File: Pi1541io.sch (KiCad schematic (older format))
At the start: 41 parts, among them J1 IEC1, J2 IEC2, J3 IEC3, J4 ExtSpkr, J5 GS3, J6 GS3, J7 GS3, J8 GS3, P1 Conn_02x20_Odd_Even, Q1 BSS138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

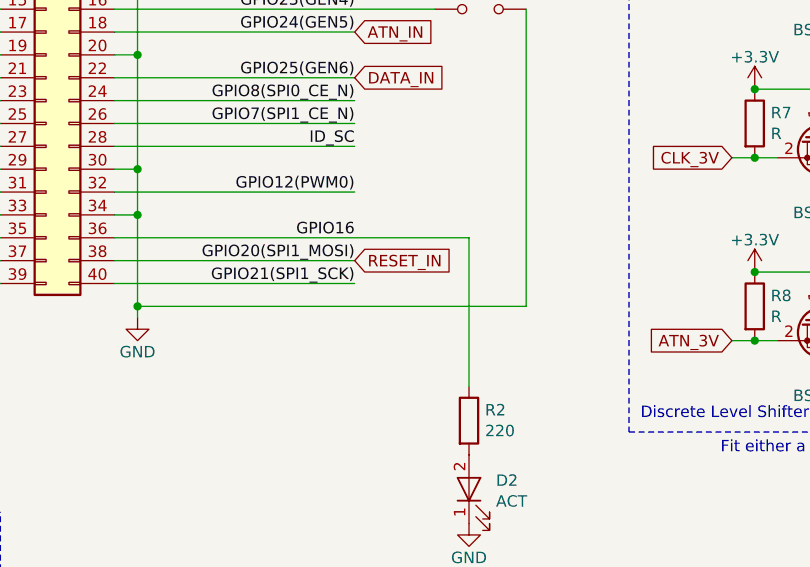
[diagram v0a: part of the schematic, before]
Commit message: Added SRQ label.
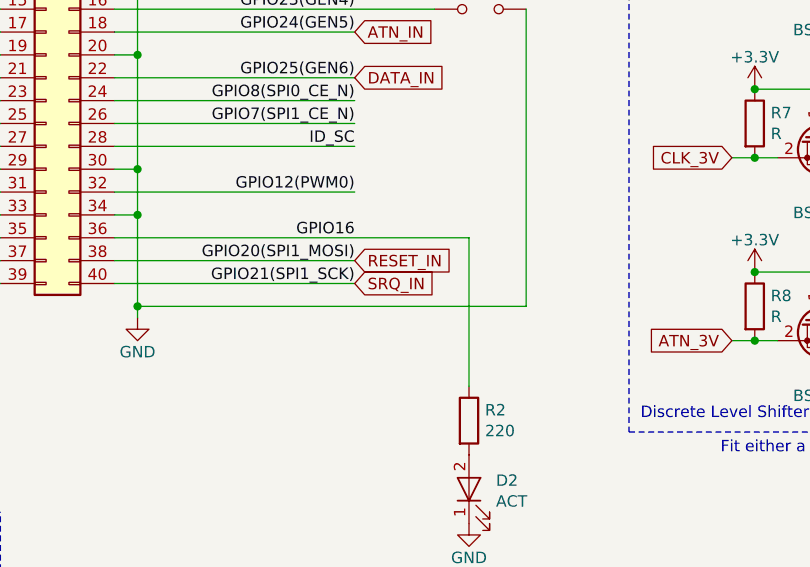
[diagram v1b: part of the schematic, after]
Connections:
- net GPIO21(SPI1_SCK) renamed SRQ_IN
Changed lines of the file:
@@
 Text Notes 6650 4050 0    50   ~ 0
 Fit either a compatible level shifter module OR the discrete components!
+Text GLabel 5050 3300 2    50   Input ~ 0
+SRQ_IN
 $EndSCHEMATC

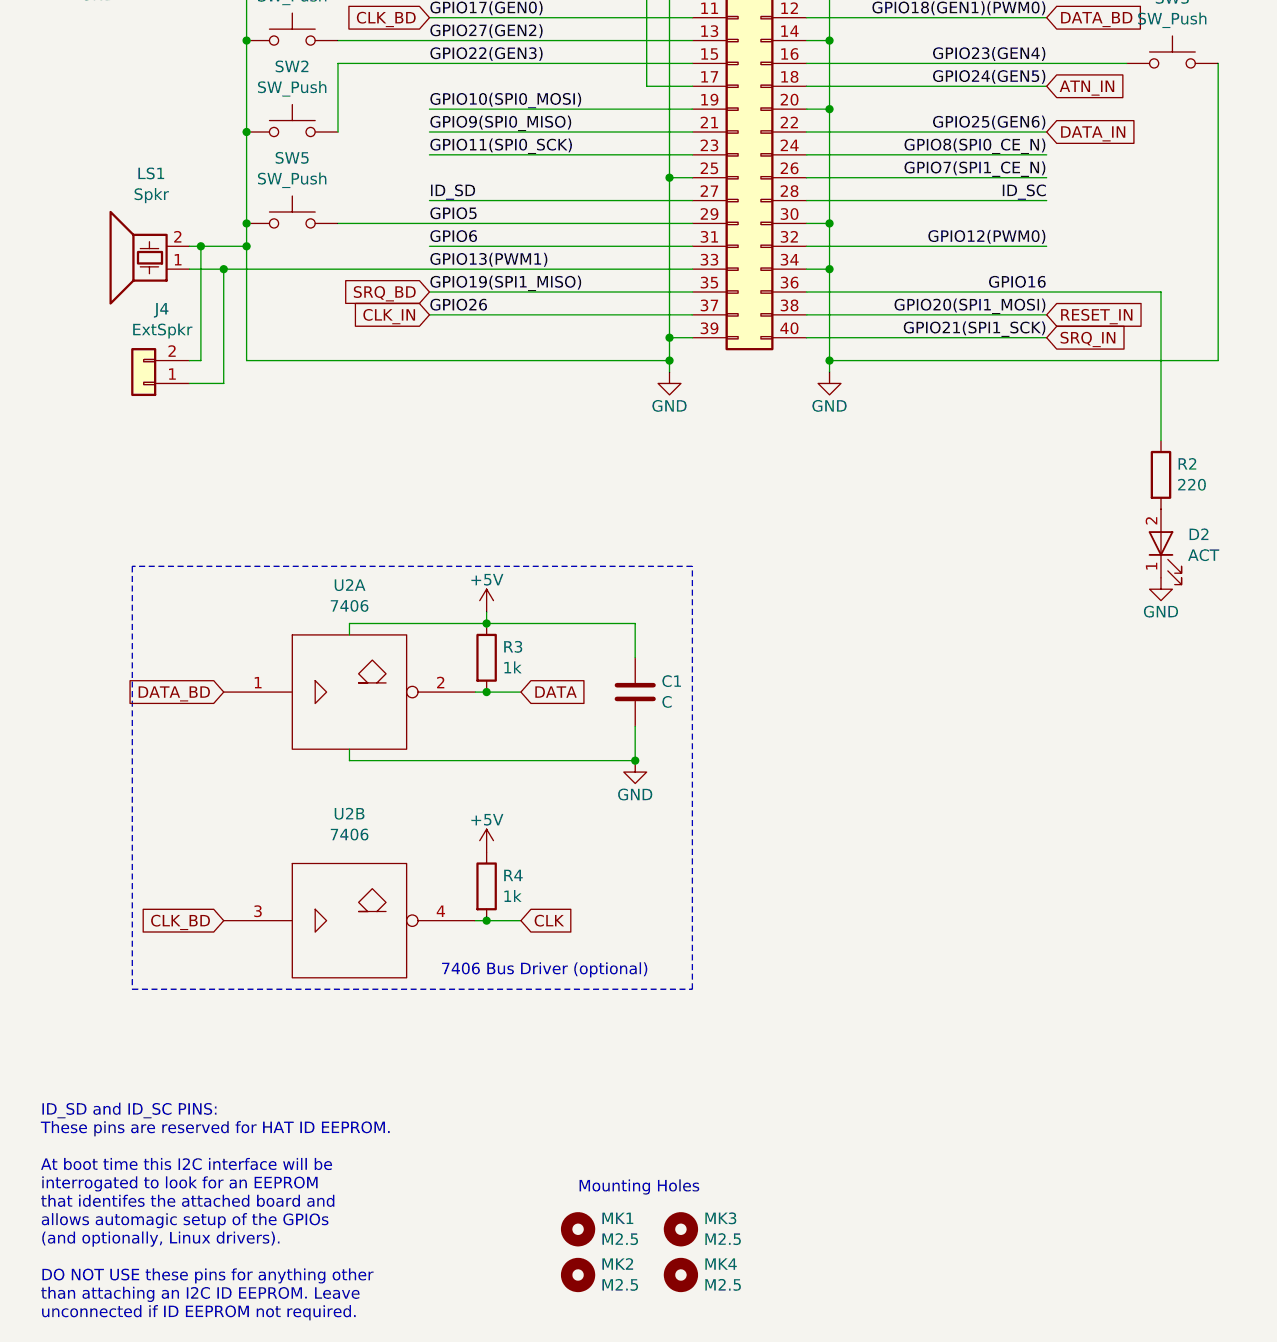
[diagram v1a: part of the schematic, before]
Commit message: Added optional components for reserved SRQ pins.
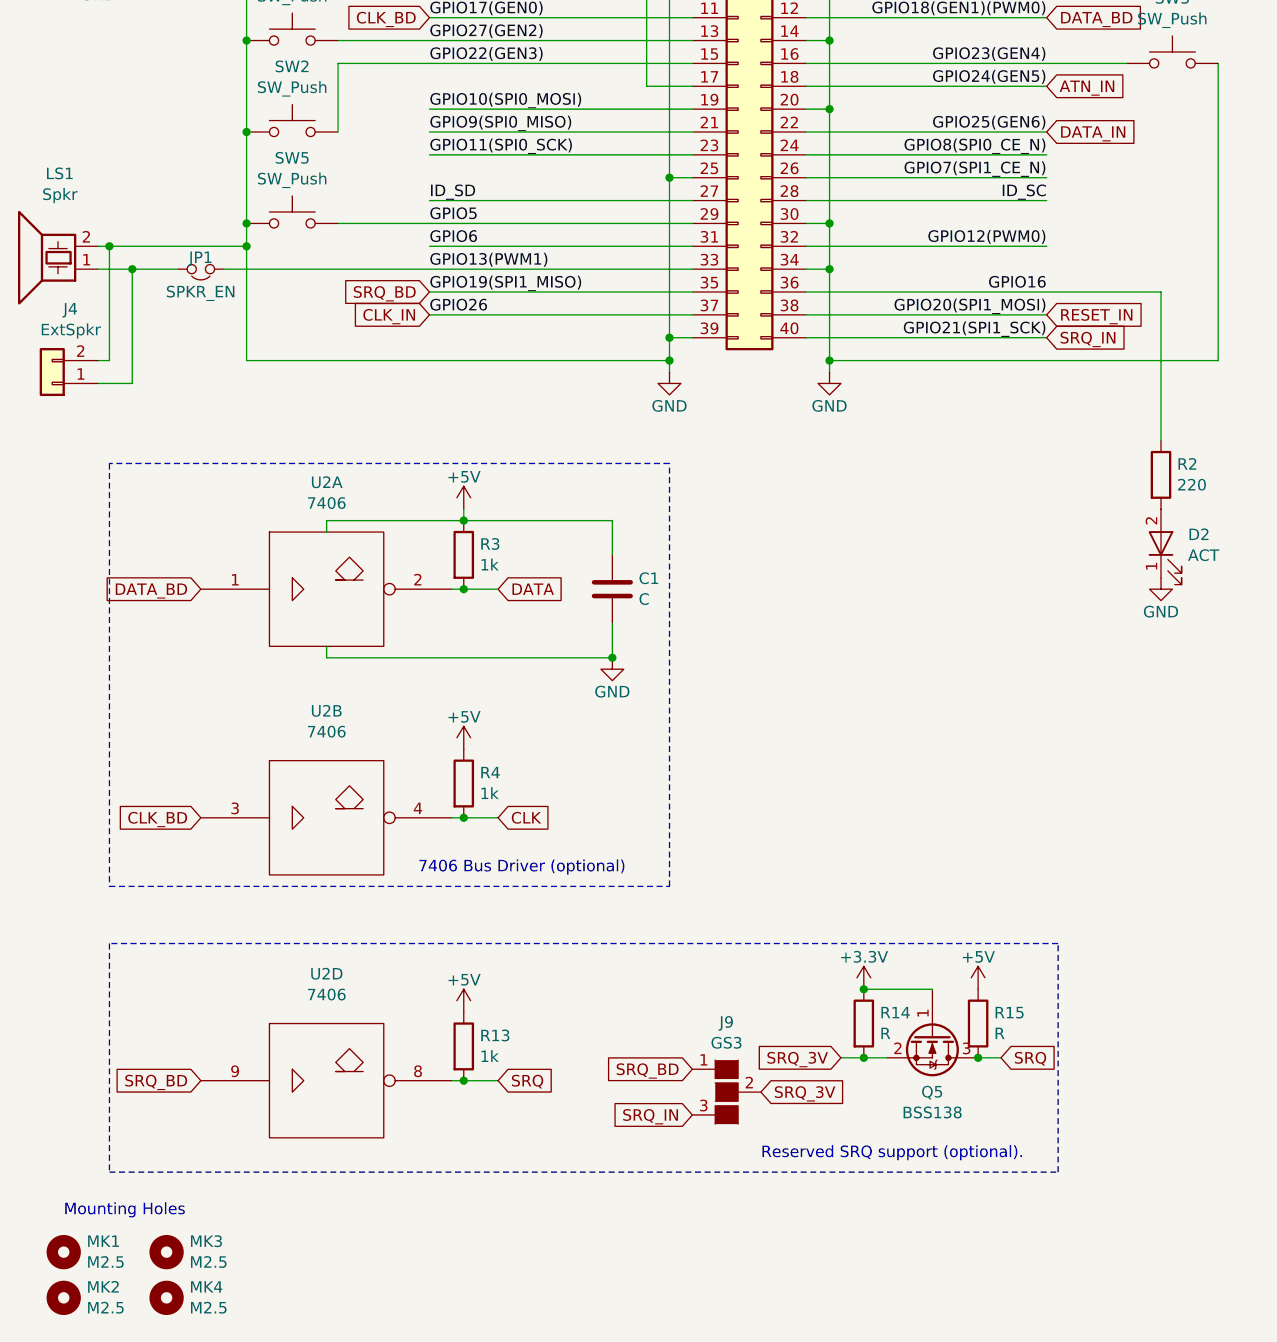
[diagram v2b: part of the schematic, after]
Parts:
- added J9: GS3, Connectors:GS3, symbol conn:GS3
- added JP1: SPKR_EN, Pin_Headers:Pin_Header_Straight_1x02_Pitch2.54mm, symbol device:Jumper_NC_Small
- added Q5: BSS138, TO_SOT_Packages_SMD:SOT-23, symbol Transistor:BSS138
- added R13: 1k, Resistors_SMD:R_0805_HandSoldering, symbol device:R
- added R14, R15: R, Resistors_SMD:R_0805, symbol device:R
- added unit 4 of U2
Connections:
- net +3V3: now also Q5.1 (G), R14.1
- net +5V: now also R13.1, R15.1, U2.14 (Vcc)
- net GND: now also U2.7 (Gnd)
- net GPIO13(PWM1): now also JP1.1; no longer J4.1 (Pin_1), LS1.1
- net SRQ: now also Q5.3 (D), R13.2, R15.2, U2.8
- net SRQ_BD: now also J9.1 (G1), U2.9
- net SRQ_IN: now also J9.3 (G3)
- new net: J4.1 (Pin_1), JP1.2, LS1.1
- new net SRQ_3V: J9.2 (G2), Q5.2 (S), R14.2
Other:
- note added: "Reserved SRQ support (optional)."
- note removed: "ID_SD and ID_SC PINS:\nThese pins are reserved for HAT ID EEPROM.\n\nAt boot time this I2C interface will be\ninterrogated to look for an EEPROM\nthat identifes the attached board and\nallows automagic setup of the GPIOs\n(and optionally, Linux drivers).\n\nDO NOT USE these pins for anything other\nthan attaching an I2C ID EEPROM. Leave\nunconnected if ID EEPROM not required."
- moved on the sheet: C1, J4, LS1, MK1, MK2, MK3, MK4, R3, R4, U2A, U2B

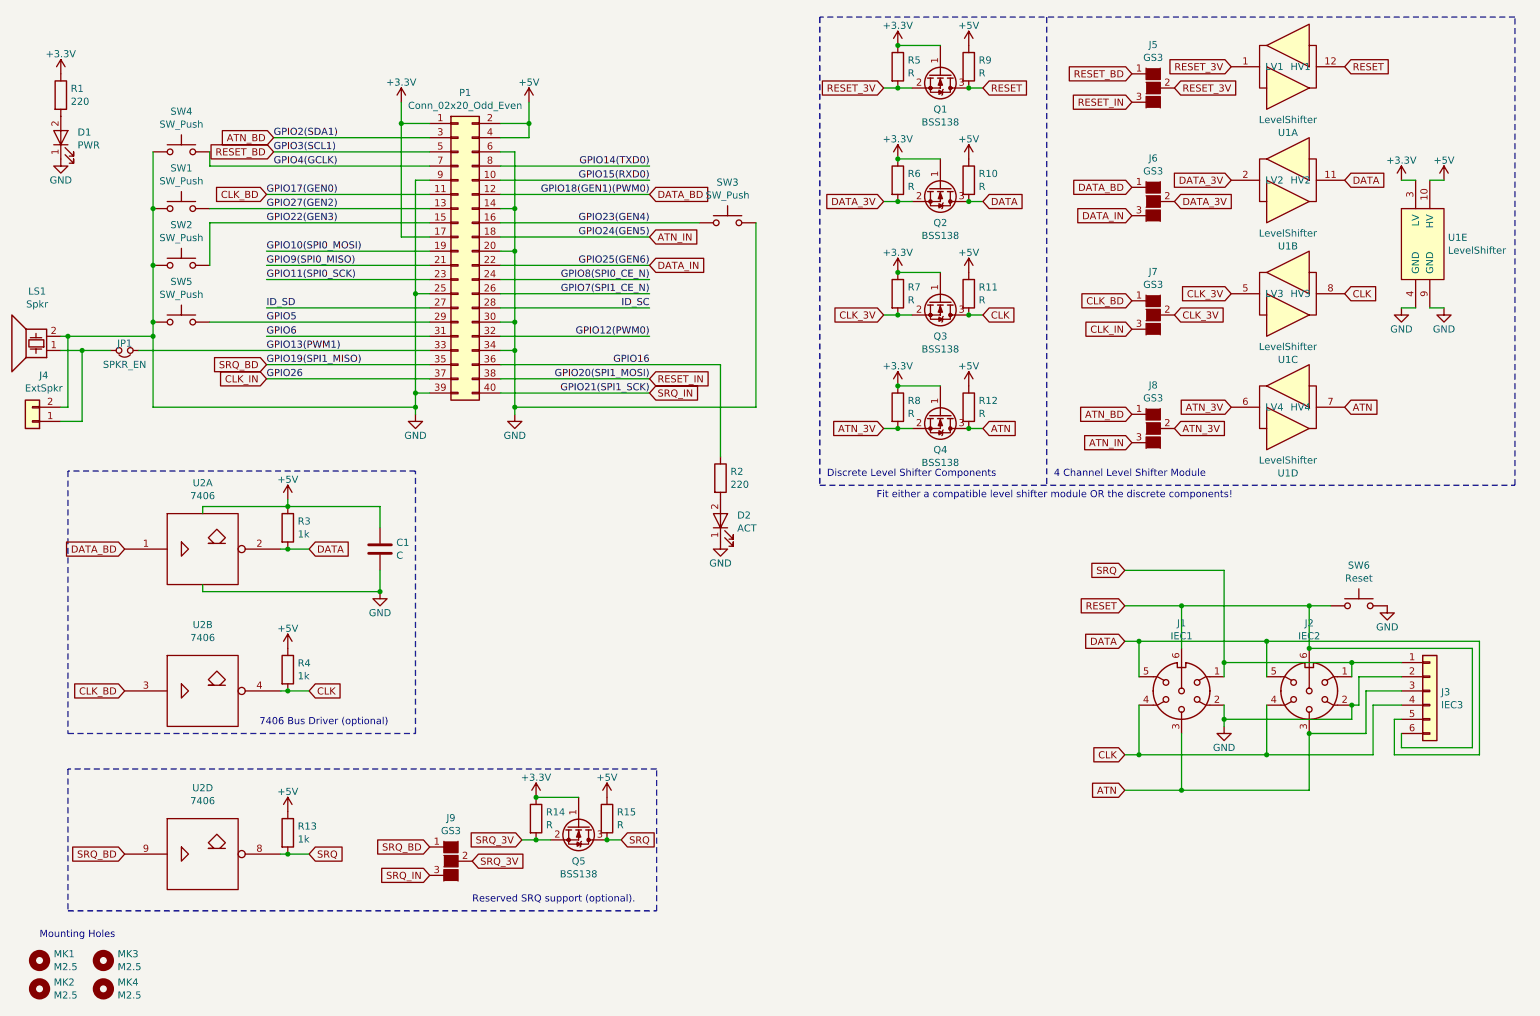
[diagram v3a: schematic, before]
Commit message: Added missing values.
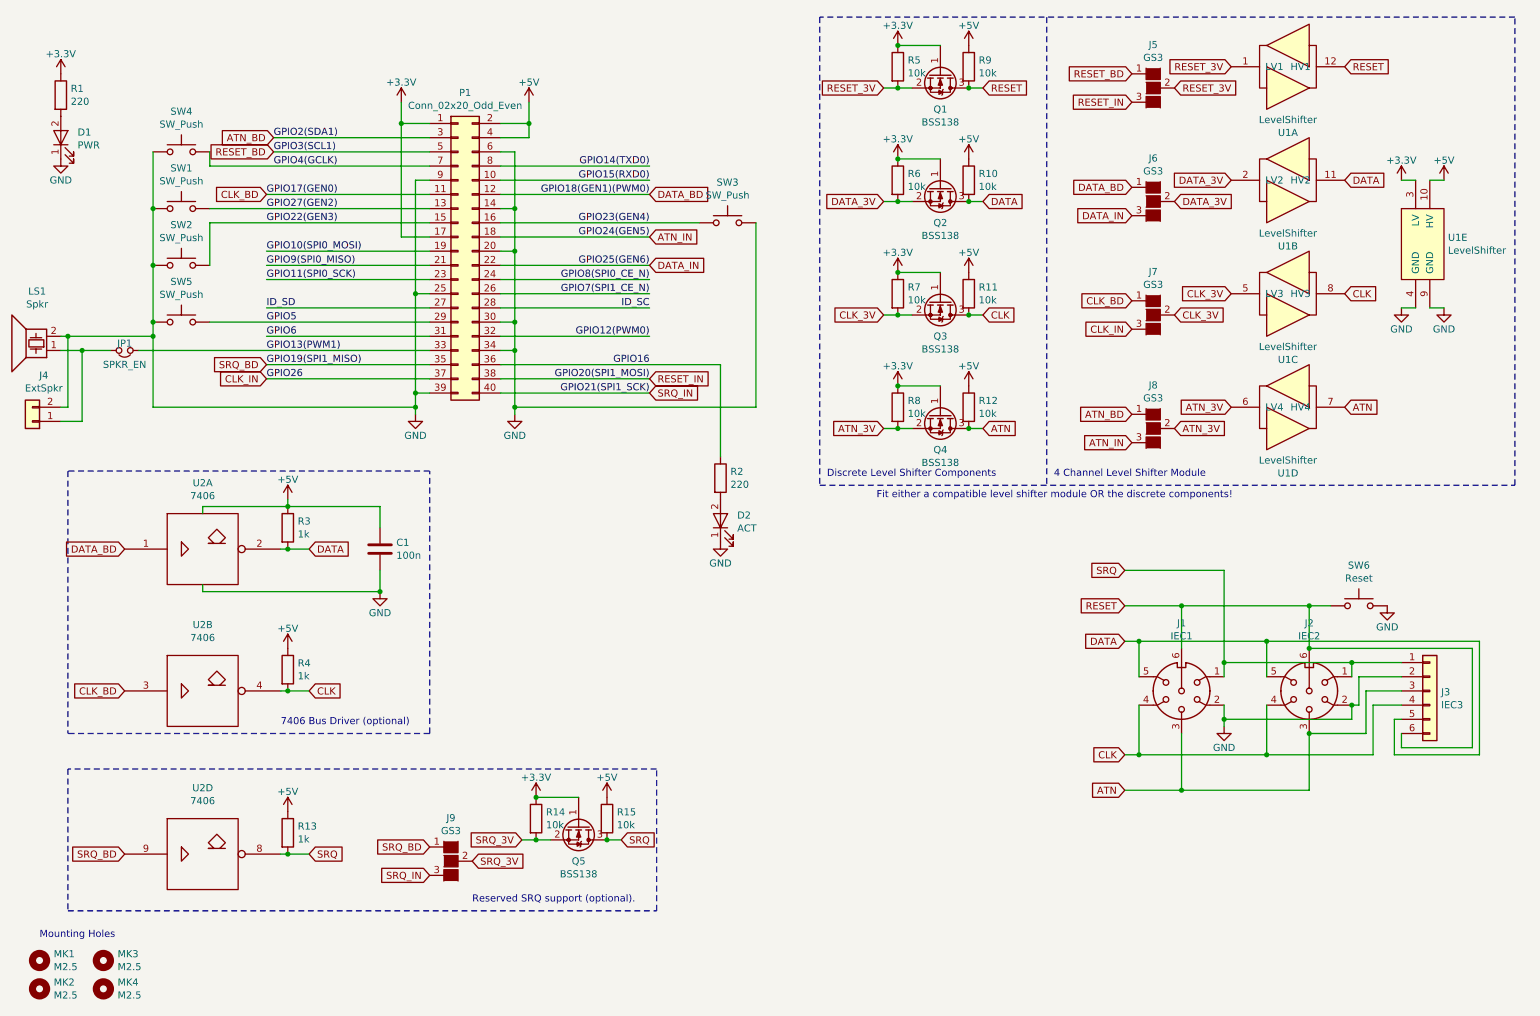
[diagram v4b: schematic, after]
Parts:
- C1: value C -> 100n
- R10, R11, R12, R14, R15, R5, R6, R7, R8, R9: value R -> 10k
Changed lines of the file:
@@
 P 3150 4400
 F 0 "C1" H 3265 4446 50  0000 L CNN
-F 1 "C" H 3265 4355 50  0000 L CNN
+F 1 "100n" H 3265 4355 50  0000 L CNN
 F 2 "Capacitors_THT:C_Disc_D3.0mm_W1.6mm_P2.50mm" H 3188 4250 50  0001 C CNN
 F 3 "" H 3150 4400 50  0001 C CNN
@@
 P 6800 1000
 F 0 "R5" H 6870 1046 50  0000 L CNN
-F 1 "R" H 6870 955 50  0000 L CNN
+F 1 "10k" H 6870 955 50  0000 L CNN
 F 2 "Resistors_SMD:R_0805" V 6730 1000 50  0001 C CNN
 F 3 "" H 6800 1000 50  0001 C CNN
@@
 P 7300 1000
 F 0 "R9" H 7370 1046 50  0000 L CNN
-F 1 "R" H 7370 955 50  0000 L CNN
+F 1 "10k" H 7370 955 50  0000 L CNN
 F 2 "Resistors_SMD:R_0805" V 7230 1000 50  0001 C CNN
 F 3 "" H 7300 1000 50  0001 C CNN
@@
 P 6800 1800
 F 0 "R6" H 6870 1846 50  0000 L CNN
-F 1 "R" H 6870 1755 50  0000 L CNN
+F 1 "10k" H 6870 1755 50  0000 L CNN
 F 2 "Resistors_SMD:R_0805" V 6730 1800 50  0001 C CNN
 F 3 "" H 6800 1800 50  0001 C CNN
@@
 P 7300 1800
 F 0 "R10" H 7370 1846 50  0000 L CNN
-F 1 "R" H 7370 1755 50  0000 L CNN
+F 1 "10k" H 7370 1755 50  0000 L CNN
 F 2 "Resistors_SMD:R_0805" V 7230 1800 50  0001 C CNN
 F 3 "" H 7300 1800 50  0001 C CNN
@@
 P 6800 2600
 F 0 "R7" H 6870 2646 50  0000 L CNN
-F 1 "R" H 6870 2555 50  0000 L CNN
+F 1 "10k" H 6870 2555 50  0000 L CNN
 F 2 "Resistors_SMD:R_0805" V 6730 2600 50  0001 C CNN
 F 3 "" H 6800 2600 50  0001 C CNN
@@
 P 7300 2600
 F 0 "R11" H 7370 2646 50  0000 L CNN
-F 1 "R" H 7370 2555 50  0000 L CNN
+F 1 "10k" H 7370 2555 50  0000 L CNN
 F 2 "Resistors_SMD:R_0805" V 7230 2600 50  0001 C CNN
 F 3 "" H 7300 2600 50  0001 C CNN
@@
 P 6800 3400
 F 0 "R8" H 6870 3446 50  0000 L CNN
-F 1 "R" H 6870 3355 50  0000 L CNN
+F 1 "10k" H 6870 3355 50  0000 L CNN
 F 2 "Resistors_SMD:R_0805" V 6730 3400 50  0001 C CNN
 F 3 "" H 6800 3400 50  0001 C CNN
@@
 P 7300 3400
 F 0 "R12" H 7370 3446 50  0000 L CNN
-F 1 "R" H 7370 3355 50  0000 L CNN
+F 1 "10k" H 7370 3355 50  0000 L CNN
 F 2 "Resistors_SMD:R_0805" V 7230 3400 50  0001 C CNN
 F 3 "" H 7300 3400 50  0001 C CNN
@@
 Discrete Level Shifter Components
 Wire Notes Line
-	3400 3850 950  3850
-Wire Notes Line
 	950  3850 950  5700
 Wire Notes Line
-	950  5700 3400 5700
-Wire Notes Line
-	3400 5700 3400 3850
-Text Notes 2300 5650 0    50   ~ 0
+	3500 5700 3500 3850
+Text Notes 2450 5650 0    50   ~ 0
 7406 Bus Driver (optional)
 Text Notes 6650 4050 0    50   ~ 0
@@
 P 4250 6300
 F 0 "R14" H 4320 6346 50  0000 L CNN
-F 1 "R" H 4320 6255 50  0000 L CNN
+F 1 "10k" H 4320 6255 50  0000 L CNN
 F 2 "Resistors_SMD:R_0805" V 4180 6300 50  0001 C CNN
 F 3 "" H 4250 6300 50  0001 C CNN
@@
 P 4750 6300
 F 0 "R15" H 4820 6346 50  0000 L CNN
-F 1 "R" H 4820 6255 50  0000 L CNN
+F 1 "10k" H 4820 6255 50  0000 L CNN
 F 2 "Resistors_SMD:R_0805" V 4680 6300 50  0001 C CNN
 F 3 "" H 4750 6300 50  0001 C CNN
@@
 Text Notes 3800 6900 0    50   ~ 0
 Reserved SRQ support (optional).
+Wire Notes Line
+	3500 3850 950  3850
+Wire Notes Line
+	3500 5700 950  5700
 $EndSCHEMATC

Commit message: Use wider footprint for cap.
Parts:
- C1: footprint Capacitors_THT:C_Disc_D3.0mm_W1.6mm_P2.50mm -> Capacitors_THT:C_Disc_D4.3mm_W1.9mm_P5.00mm
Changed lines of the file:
@@
 F 0 "C1" H 3265 4446 50  0000 L CNN
 F 1 "100n" H 3265 4355 50  0000 L CNN
-F 2 "Capacitors_THT:C_Disc_D3.0mm_W1.6mm_P2.50mm" H 3188 4250 50  0001 C CNN
+F 2 "Capacitors_THT:C_Disc_D4.3mm_W1.9mm_P5.00mm" H 3188 4250 50  0001 C CNN
 F 3 "" H 3150 4400 50  0001 C CNN
 	1    3150 4400

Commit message: Added I2C display connector.
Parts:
- added J10: SDA, Connectors:GS3, symbol conn:GS3
- added J11: SCL, Connectors:GS3, symbol conn:GS3
- added J12: I2C, Socket_Strips:Socket_Strip_Straight_1x04_Pitch2.54mm, symbol Connector:Conn_01x04
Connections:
- net labels added: I2C0_SCL, I2C0_SDA, I2C1_SCL, I2C1_SDA
- wire segments 156 -> 172
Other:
- note added: "I2C Display Connector"
- note added: "Reserved SRQ support (optional)"
- note removed: "Reserved SRQ support (optional)."
- moved on the sheet: D1, D2, J4, JP1, LS1, P1, R1, R2, SW1, SW2, SW3, SW4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
